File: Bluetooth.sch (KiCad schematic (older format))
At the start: 5 parts, among them U18 MCP112, U19 RN4871-I

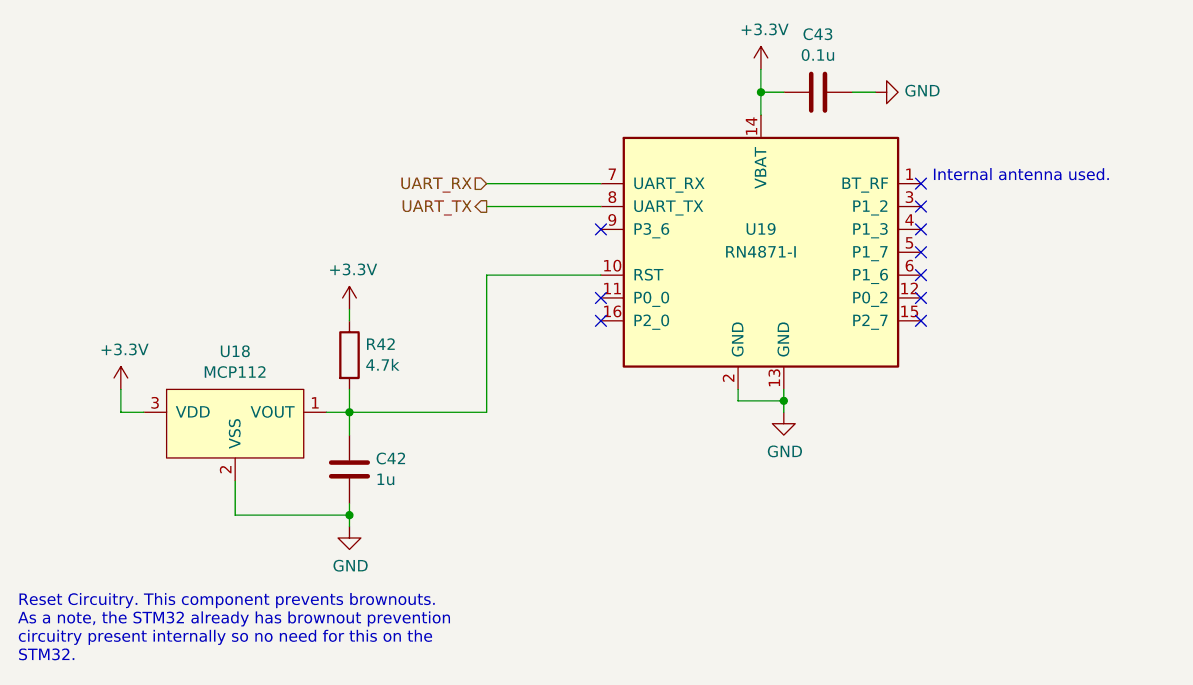
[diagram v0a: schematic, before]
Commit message: Updates BAS70-04 footprint for Contactor auxillary interface
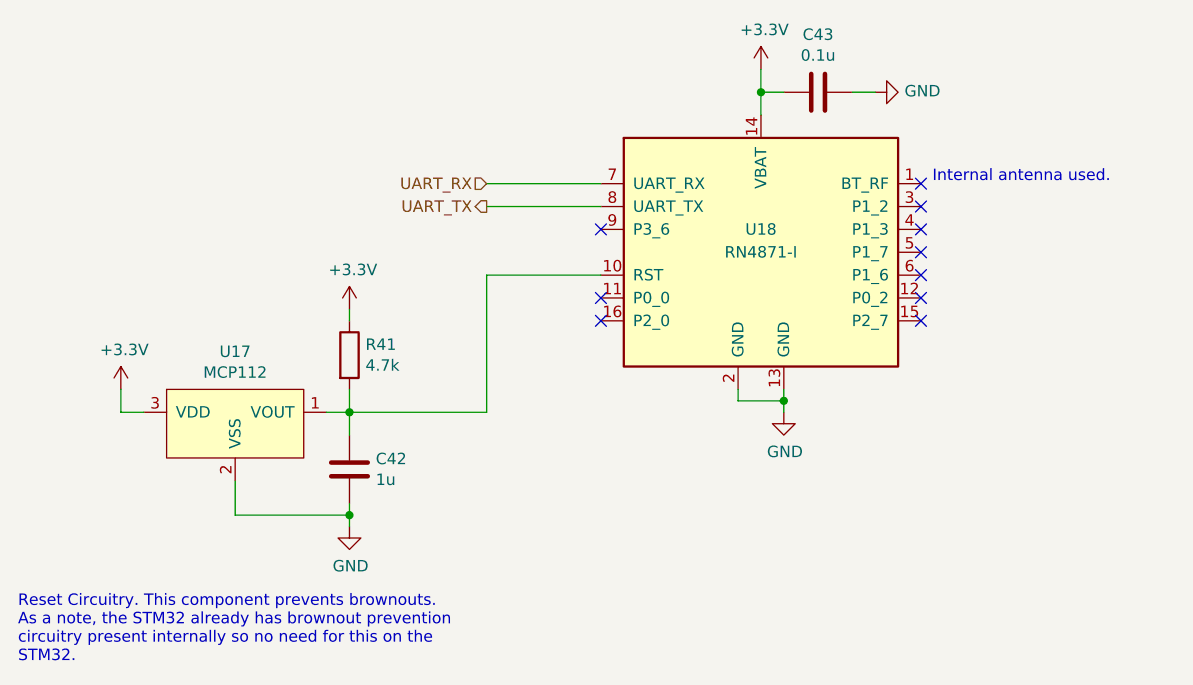
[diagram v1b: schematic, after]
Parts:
- renumbered R42 to R41, U18 to U17, U19 to U18
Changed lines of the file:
@@
 $EndDescr
 $Comp
-L RF_Bluetooth:RN4871 U19
+L RF_Bluetooth:RN4871 U18
 U 1 1 5F24C128
 P 5800 3300
-F 0 "U19" H 5800 3400 50  0000 C CNN
+F 0 "U18" H 5800 3400 50  0000 C CNN
 F 1 "RN4871-I" H 5800 3300 50  0000 C CNN
 F 2 "RF_Module:Microchip_RN4871" H 5800 2600 50  0001 C CNN
@@
 $EndComp
 $Comp
-L power:+3.3V #PWR0101
+L power:+3.3V #PWR0103
 U 1 1 5F24CC20
 P 5800 2500
-F 0 "#PWR0101" H 5800 2350 50  0001 C CNN
+F 0 "#PWR0103" H 5800 2350 50  0001 C CNN
 F 1 "+3.3V" H 5815 2673 50  0000 C CNN
 F 2 "" H 5800 2500 50  0001 C CNN
@@
 	5800 2600 5800 2700
 $Comp
-L power:GND #PWR0103
+L power:GND #PWR0105
 U 1 1 5F24E813
 P 6300 2600
-F 0 "#PWR0103" H 6300 2350 50  0001 C CNN
+F 0 "#PWR0105" H 6300 2350 50  0001 C CNN
 F 1 "GND" V 6305 2472 50  0000 R CNN
 F 2 "" H 6300 2600 50  0001 C CNN
@@
 NoConn ~ 5100 3600
 $Comp
-L power:GND #PWR0102
+L power:GND #PWR0104
 U 1 1 5F2507B7
 P 5900 4000
-F 0 "#PWR0102" H 5900 3750 50  0001 C CNN
+F 0 "#PWR0104" H 5900 3750 50  0001 C CNN
 F 1 "GND" H 5905 3827 50  0000 C CNN
 F 2 "" H 5900 4000 50  0001 C CNN
@@
 	5100 3100 4600 3100
 $Comp
-L utsvt-bps:MCP112 U18
+L utsvt-bps:MCP112 U17
 U 1 1 5F286E74
 P 3500 3900
-F 0 "U18" H 3500 4065 50  0000 C CNN
+F 0 "U17" H 3500 4065 50  0000 C CNN
 F 1 "MCP112" H 3500 3974 50  0000 C CNN
 F 2 "Package_TO_SOT_SMD:SOT-23" H 3500 3900 50  0001 C CNN
@@
 $EndComp
 $Comp
-L power:+3.3V #PWR098
+L power:+3.3V #PWR0100
 U 1 1 5F2892CC
 P 3000 3900
-F 0 "#PWR098" H 3000 3750 50  0001 C CNN
+F 0 "#PWR0100" H 3000 3750 50  0001 C CNN
 F 1 "+3.3V" H 3015 4073 50  0000 C CNN
 F 2 "" H 3000 3900 50  0001 C CNN
@@
 	3000 4000 3100 4000
 $Comp
-L Device:R R42
+L Device:R R41
 U 1 1 5F28A0A0
 P 4000 3750
-F 0 "R42" H 4070 3796 50  0000 L CNN
+F 0 "R41" H 4070 3796 50  0000 L CNN
 F 1 "4.7k" H 4070 3705 50  0000 L CNN
 F 2 "Resistor_SMD:R_0805_2012Metric" V 3930 3750 50  0001 C CNN
@@
 Connection ~ 4000 4000
 $Comp
-L power:GND #PWR0100
+L power:GND #PWR0102
 U 1 1 5F28AD68
 P 4000 4500
-F 0 "#PWR0100" H 4000 4250 50  0001 C CNN
+F 0 "#PWR0102" H 4000 4250 50  0001 C CNN
 F 1 "GND" H 4005 4327 50  0000 C CNN
 F 2 "" H 4000 4500 50  0001 C CNN
@@
 	4000 4450 4000 4400
 $Comp
-L power:+3.3V #PWR099
+L power:+3.3V #PWR0101
 U 1 1 5F28BC6F
 P 4000 3550
-F 0 "#PWR099" H 4000 3400 50  0001 C CNN
+F 0 "#PWR0101" H 4000 3400 50  0001 C CNN
 F 1 "+3.3V" H 4015 3723 50  0000 C CNN
 F 2 "" H 4000 3550 50  0001 C CNN
